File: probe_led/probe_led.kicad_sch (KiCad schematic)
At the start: 39 parts

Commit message: - add led pcb
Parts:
- removed D12, D4, D8, IR1, IR10, IR11, IR12, IR2, IR3, IR4, IR5, IR6, IR7, IR8, IR9: LED, LED_SMD:LED_0603_1608Metric_Pad1.05x0.95mm_HandSolder, symbol Device:LED
- removed R12, R4, R8: R, Resistor_SMD:R_0603_1608Metric_Pad0.98x0.95mm_HandSolder, symbol Device:R
- added U1, U2, U3: IRM-H638T_TR2, IRM-H638T:IRM-H638T&slash_TR2_EVE-L, symbol IRM-H638T-TR2:IRM-H638T_TR2
- D1, D10, D11, D2, D3, D5, D6, D7, D9: footprint LED_SMD:LED_0603_1608Metric_Pad1.05x0.95mm_HandSolder -> LED_SMD:LED_1206_3216Metric_Pad1.42x1.75mm_HandSolder
- renumbered 5V to 5V1, GND to GND1, IR to IR1
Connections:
- net +5V: now also U1.4, U2.4, U3.4
- net GND: now also U1.1, U1.2, U2.1, U2.2, U3.1, U3.2
- net at IR1.1: now also U1.3, U2.3, U3.3

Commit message: - add new power version
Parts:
- removed 5V1: 5V, TestPoint:TestPoint_Pad_D1.0mm, symbol Connector:TestPoint
- added 5V: 5V, TestPoint:TestPoint_Pad_D1.0mm, symbol Connector:TestPoint
- added LED-: GND, TestPoint:TestPoint_Pad_D1.0mm, symbol Connector:TestPoint
- renumbered GND1 to IR-, IR1 to IR_D
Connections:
- net +5V: no longer names the net of D1.2 (A), D10.2 (A), D11.2 (A), D2.2 (A), D3.2 (A), D5.2 (A), D6.2 (A), D7.2 (A), D9.2 (A), U1.4, U2.4, U3.4
- net +5V: now also 5V.1
- net GND: no longer names the net of R1.2, R10.2, R11.2, R2.2, R3.2, R5.2, R6.2, R7.2, R9.2
- net GND: now also LED-.1; no longer IR-.1, U1.1, U1.2, U2.1, U2.2, U3.1, U3.2
- new net: IR-.1, U1.1, U1.2, U2.1, U2.2, U3.1, U3.2
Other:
- moved on the sheet: IR-, IR_D

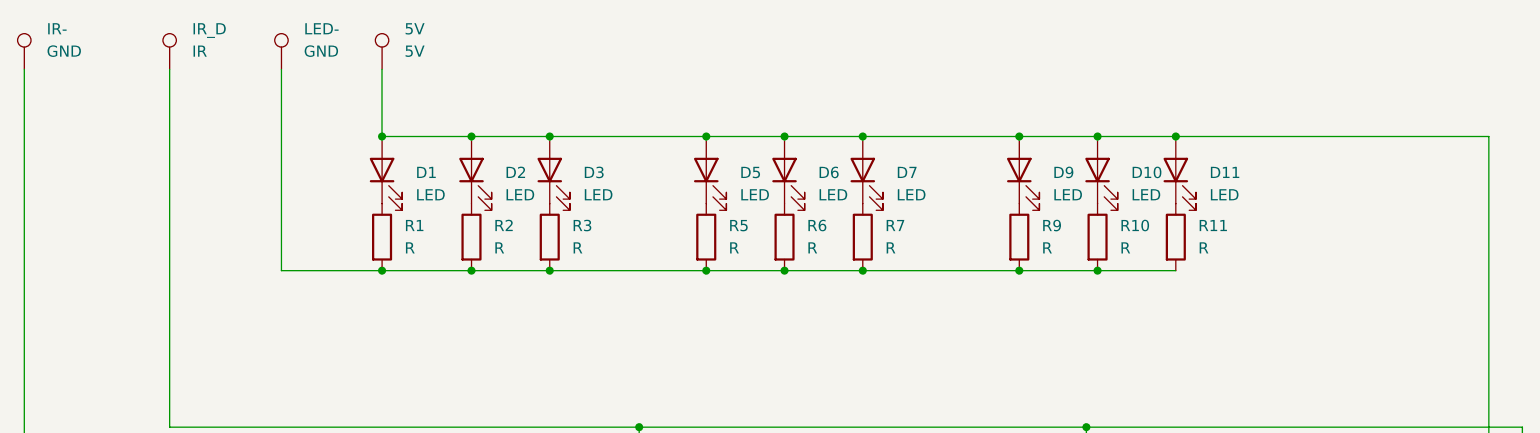
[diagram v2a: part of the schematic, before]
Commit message: -add new size led
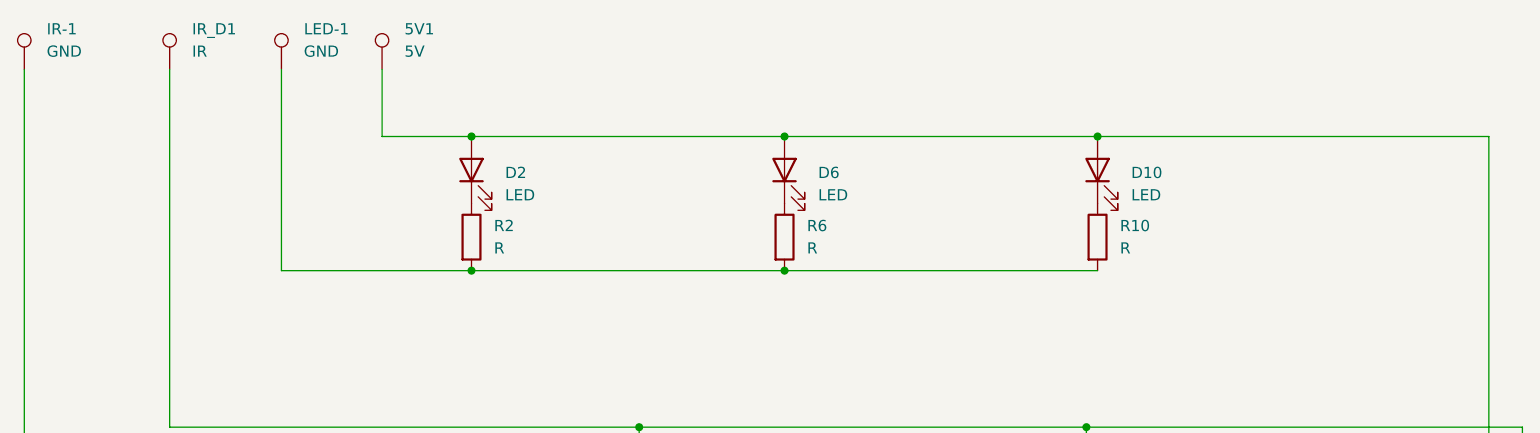
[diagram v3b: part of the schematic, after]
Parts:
- removed D1, D11, D3, D5, D7, D9: LED, LED_SMD:LED_1206_3216Metric_Pad1.42x1.75mm_HandSolder, symbol Device:LED
- removed R1, R11, R3, R5, R7, R9: R, Resistor_SMD:R_0603_1608Metric_Pad0.98x0.95mm_HandSolder, symbol Device:R
- renumbered 5V to 5V1, IR- to IR-1, IR_D to IR_D1, LED- to LED-1

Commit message: -add new version for transmitter
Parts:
- added J1: Conn_01x05_Pin, symbol Connector:Conn_01x05_Pin
- added J2: Conn_01x03_Pin, symbol Connector:Conn_01x03_Pin
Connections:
- net at IR-1.1, U1.1, U1.2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: now also J1.4 (Pin_4)
- net at IR_D1.1, U1.3, U2.3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: now also J1.3 (Pin_3)
- net at 5V1.1, D10.2 (A), D2.2 (A)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: now also J1.1 (Pin_1), J2.3 (Pin_3)
- net at LED-1.1, R10.2, R2.2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: now also J1.2 (Pin_2)

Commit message: -prepare for production
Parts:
- removed J1: Conn_01x05_Pin, symbol Connector:Conn_01x05_Pin
- removed J2: Conn_01x03_Pin, symbol Connector:Conn_01x03_Pin
- added J3: Conn_01x06, Library:FPC_4pin_0.5mm_fingers, symbol Connector_Generic:Conn_01x06
- 3V3: renamed from 5V1; value 5V -> 33V
- renumbered LED-1 to IRLED_POW1, IR_D1 to IRREC_DATA1, IR-1 to IRREC_POW1
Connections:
- net at IRREC_POW1.1, U1.1, U1.2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: now also J3.3 (Pin_3)
- net at IRREC_DATA1.1, U1.3, U2.3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: now also J3.4 (Pin_4)
- net +3.3V: now reaches 3V3.1, D10.2 (A), D2.2 (A), D6.2 (A), U1.4, U2.4, U3.4
- net +3.3V: now also J3.1 (Pin_1)
- net at IRLED_POW1.1, R10.2, R2.2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: now also J3.2 (Pin_2)
